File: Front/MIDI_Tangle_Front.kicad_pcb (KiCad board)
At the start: 2 copper layers, 40.3 x 128.5 mm, 28 parts, among them J1 Screw_Terminal_01x01, J10 Screw_Terminal_01x01, J11 Screw_Terminal_01x01, J12 Screw_Terminal_01x01, J13 Screw_Terminal_01x01, J14 Screw_Terminal_01x01, J15 Screw_Terminal_01x01, J16 Screw_Terminal_01x01, J17 Screw_Terminal_01x01, J18 Screw_Terminal_01x01, J19 Screw_Terminal_01x01, J2 Screw_Terminal_01x01, J20 Screw_Terminal_01x01, J3 Screw_Terminal_01x01, J4 Screw_Terminal_01x01, J5 Screw_Terminal_01x01, J6 Screw_Terminal_01x01, J7 Screw_Terminal_01x01, J8 Screw_Terminal_01x01, J9 Screw_Terminal_01x01

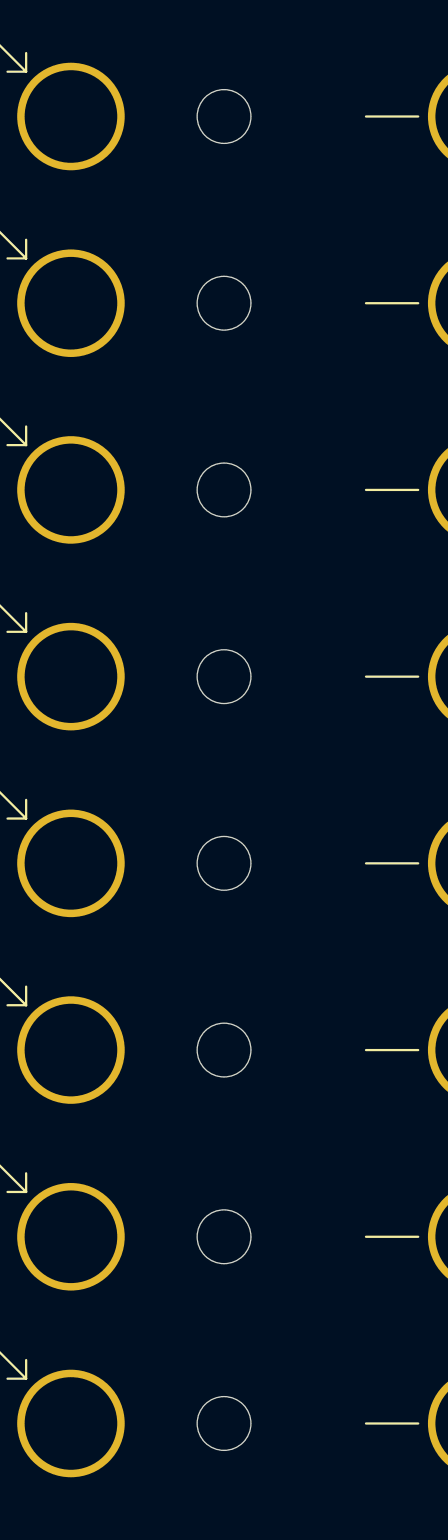
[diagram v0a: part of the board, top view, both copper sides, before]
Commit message: Add custom footprints and symbols
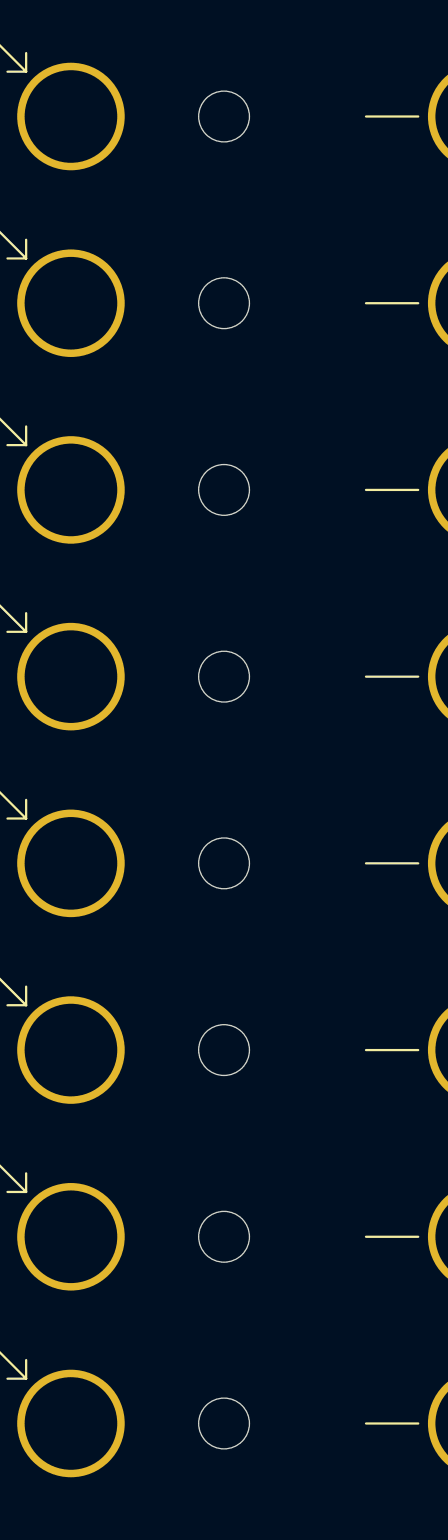
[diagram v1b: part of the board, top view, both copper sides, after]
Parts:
- H1, H2, H3, H4, H5, H6, H7, H8: footprint CustomLib:TactileHole -> Custom_FP:TactileHole
- J1, J2, J3, J4: footprint CustomLib:Wide_M3 -> Custom_FP:Wide_M3
- J10, J11, J12, J13, J14, J15, J16, J17, J18, J19, J20, J5, J6, J7, J8, J9: footprint MountingHole:MountingHole_6.2mm_M6 -> Custom_FP:MountingHole_PJ398SM
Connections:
- J1 pad 1: (no net) -> Net-(J1-Pad1)
- J2 pad 1: (no net) -> Net-(J2-Pad1)
- J3 pad 1: (no net) -> Net-(J3-Pad1)
- J4 pad 1: (no net) -> Net-(J4-Pad1)

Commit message: Update front panel
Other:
- net class Default removed
- board text added: "2"
- board text added: "M IDI TANGLE"
- board text removed: "MIDIBUS TANGLE"
